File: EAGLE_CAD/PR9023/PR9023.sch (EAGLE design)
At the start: 74 parts, among them SW1 ESWT_TL3315, U1 SI4702-C19-GMR, X1 ABS25XTAL

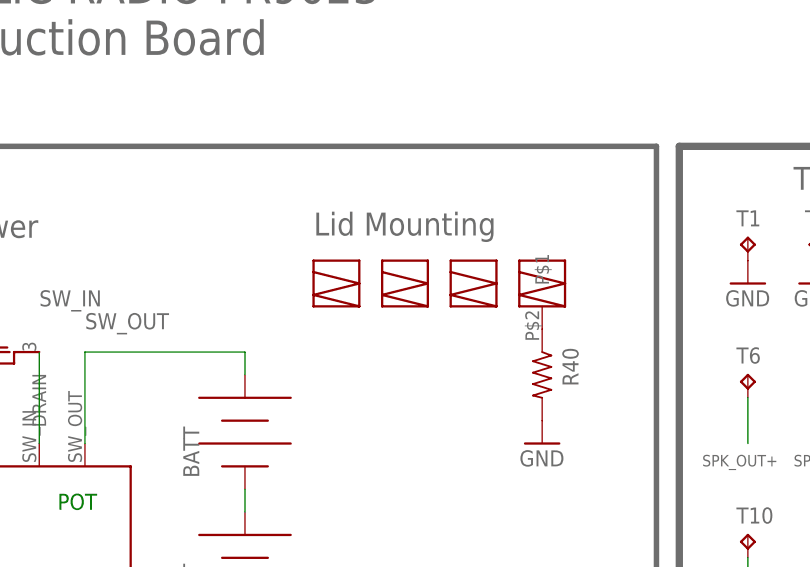
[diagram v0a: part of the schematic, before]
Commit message: first update in a while from my end
the big change here is the speaker footprint itself. i updated that to
fit Fun’s redesign. i also made some smallish changes to the board
perimeter and a few of the things inside it - mostly very small changes.
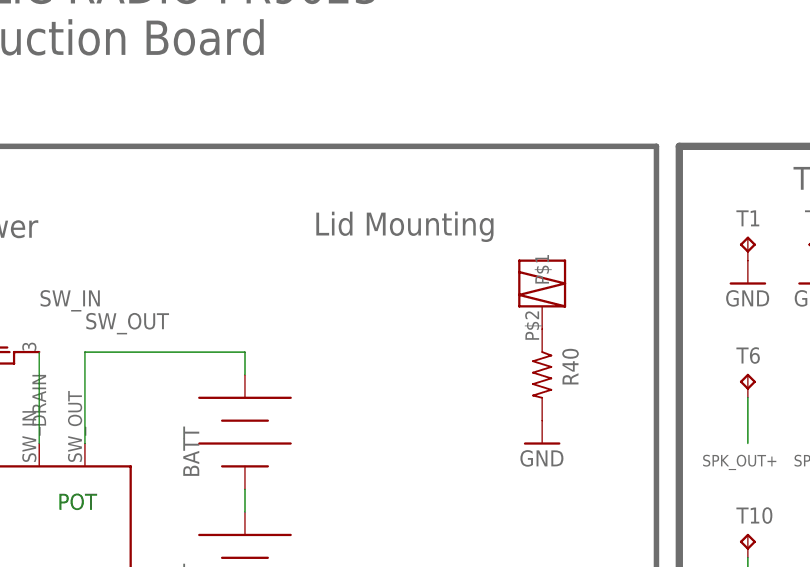
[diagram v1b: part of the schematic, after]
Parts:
- removed U$2, U$3, U$4: PEM_M3_NOPIN, PR_Parts_Library:PEM_M3_NOPIN
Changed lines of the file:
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@@
 <?xml version="1.0" encoding="utf-8"?>
 <!DOCTYPE eagle SYSTEM "eagle.dtd">
-<eagle version="6.6.0">
+<eagle version="7.5.0">
 <drawing>
 <settings>
@@
 <attribute name="MFG_PN" value="ERJ-6GEY0R00V "/>
 </part>
-<part name="U$2" library="PR_Parts_Library" deviceset="PEM_M3_NOPIN" device=""/>
-<part name="U$3" library="PR_Parts_Library" deviceset="PEM_M3_NOPIN" device=""/>
-<part name="U$4" library="PR_Parts_Library" deviceset="PEM_M3_NOPIN" device=""/>
 <part name="U$5" library="PR_Parts_Library" deviceset="PEM_M3_W/PIN" device=""/>
 </parts>
@@
 <attribute name="VALUE" x="237.49" y="24.638" size="1.778" layer="96"/>
 </instance>
-<instance part="U$2" gate="G$1" x="20.32" y="137.16"/>
-<instance part="U$3" gate="G$1" x="27.94" y="137.16"/>
-<instance part="U$4" gate="G$1" x="35.56" y="137.16"/>
 <instance part="U$5" gate="G$1" x="43.18" y="137.16"/>
 </instances>

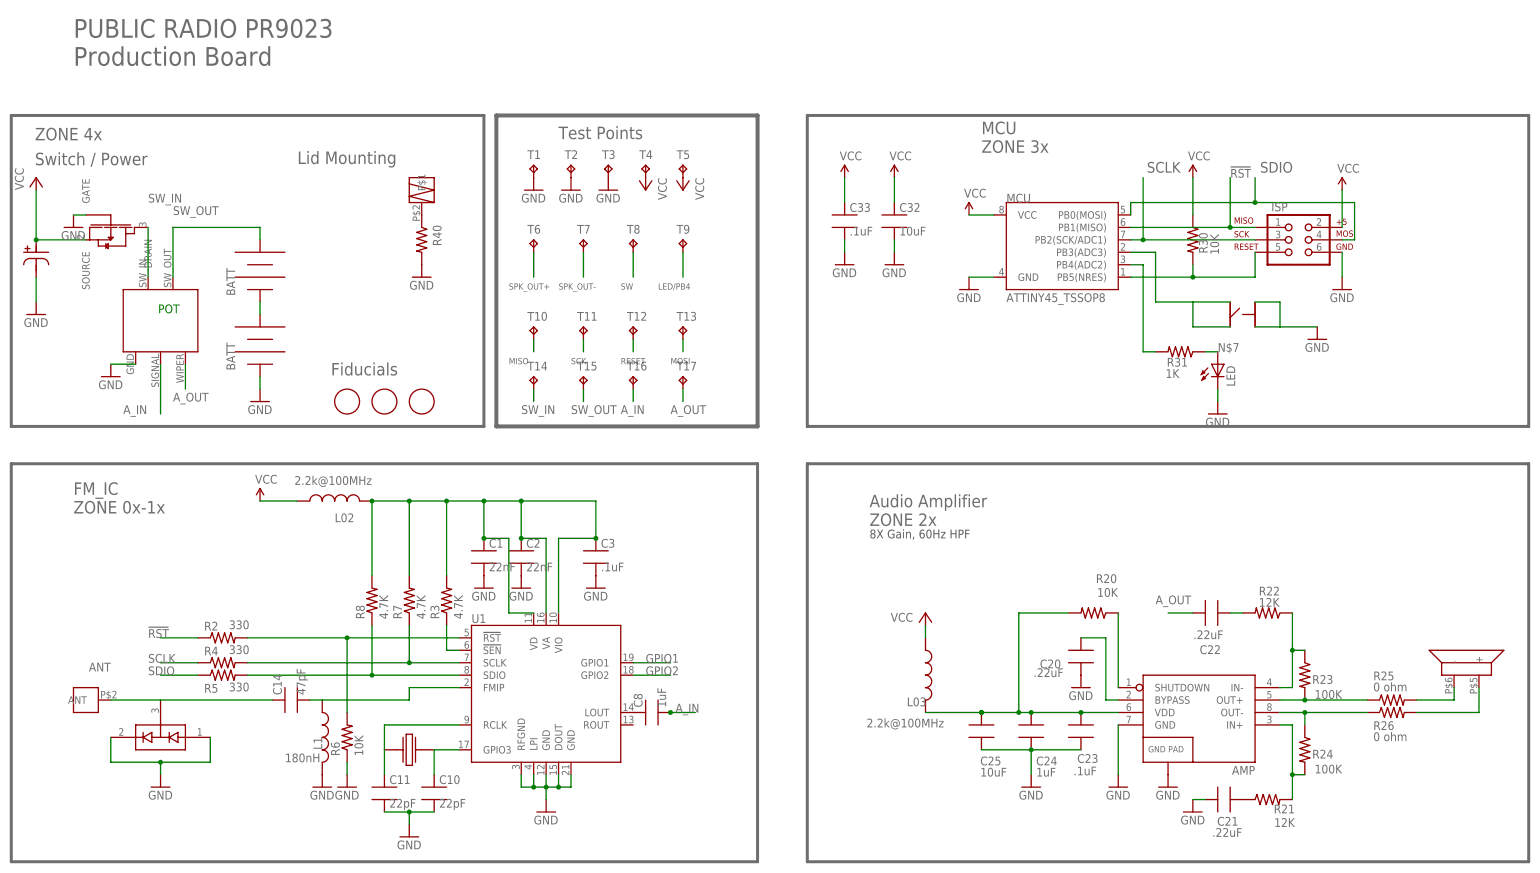
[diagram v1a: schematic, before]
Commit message: Small changes
Added ground to the speaker/lid connection
Modified board outline
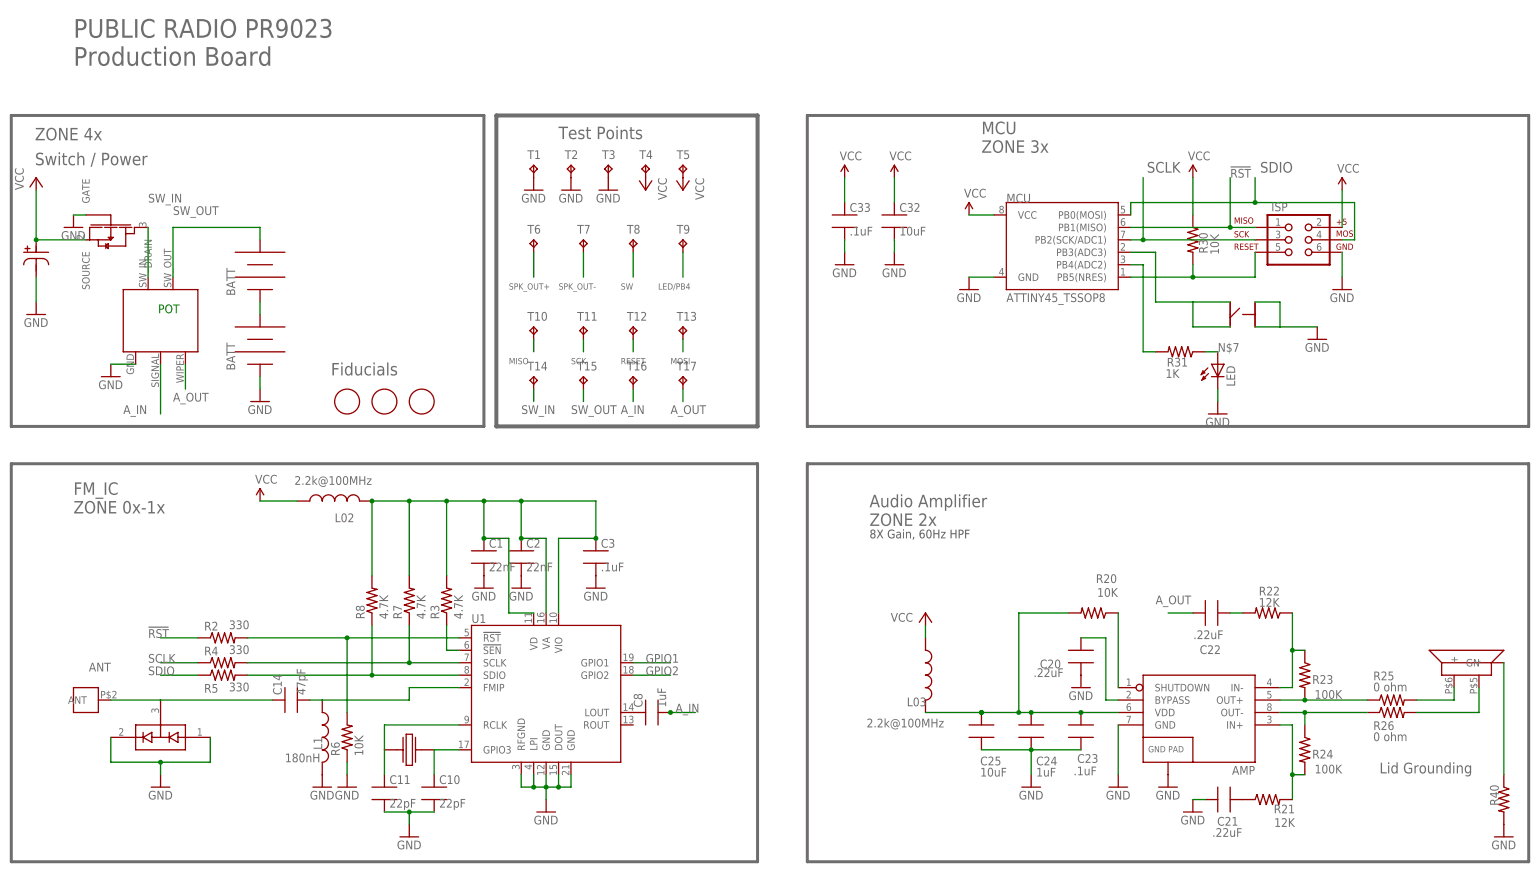
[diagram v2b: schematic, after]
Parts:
- removed U$5: PEM_M3_W/PIN, PR_Parts_Library:PEM_M3_W/PIN
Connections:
- net N$6: now also SPKR_PLACE.GN; no longer U$5.P$1
- net SPK_OUT+: now also SPKR_PLACE.+; no longer SPKR_PLACE.-
- net SPK_OUT-: now also SPKR_PLACE.-; no longer SPKR_PLACE.+
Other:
- note added: "Lid Grounding"
- note removed: "Lid Mounting"
- moved on the sheet: R40
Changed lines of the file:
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@@
 <?xml version="1.0" encoding="utf-8"?>
 <!DOCTYPE eagle SYSTEM "eagle.dtd">
-<eagle version="7.5.0">
+<eagle version="6.6.0">
 <drawing>
 <settings>
@@
 <attribute name="MFG_PN" value="ERJ-6GEY0R00V "/>
 </part>
-<part name="U$5" library="PR_Parts_Library" deviceset="PEM_M3_W/PIN" device=""/>
 </parts>
 <sheets>
@@
 ZONE 0x-1x</text>
 <text x="-35.814" y="142.24" size="2.54" layer="96">Switch / Power  </text>
-<text x="17.78" y="142.494" size="2.54" layer="96">Lid Mounting</text>
+<text x="238.76" y="18.034" size="2.1844" layer="96">Lid Grounding</text>
 <text x="134.62" y="68.58" size="2.54" layer="96">Audio Amplifier
 ZONE 2x</text>
@@
 <instance part="GND5" gate="1" x="-20.32" y="99.06"/>
 <instance part="GND2" gate="1" x="-35.56" y="111.76"/>
-<instance part="GND12" gate="1" x="43.18" y="119.38"/>
+<instance part="GND12" gate="1" x="264.16" y="5.08"/>
 <instance part="GND3" gate="1" x="-27.94" y="129.54"/>
 <instance part="MCU" gate="G$1" x="175.26" y="124.46"/>
@@
 <attribute name="VALUE" x="176.276" y="17.653" size="1.778" layer="96"/>
 </instance>
-<instance part="R40" gate="G$1" x="43.18" y="127" smashed="yes" rot="R270">
-<attribute name="NAME" x="47.2186" y="125.73" size="1.778" layer="95" rot="R90"/>
+<instance part="R40" gate="G$1" x="264.16" y="12.7" smashed="yes" rot="R270">
+<attribute name="NAME" x="263.1186" y="11.43" size="1.778" layer="95" rot="R90"/>
 </instance>
 <instance part="D1" gate="G$1" x="-10.16" y="25.4" rot="R180"/>
@@
 <attribute name="VALUE" x="237.49" y="24.638" size="1.778" layer="96"/>
 </instance>
-<instance part="U$5" gate="G$1" x="43.18" y="137.16"/>
 </instances>
 <busses>
@@
 <wire x1="246.38" y1="33.02" x2="254" y2="33.02" width="0.1524" layer="91"/>
 <pinref part="R25" gate="G$1" pin="2"/>
-<pinref part="SPKR_PLACE" gate="G$1" pin="-"/>
+<pinref part="SPKR_PLACE" gate="G$1" pin="+"/>
 <wire x1="254" y1="33.02" x2="254" y2="35.56" width="0.1524" layer="91"/>
 </segment>
@@
 <segment>
 <pinref part="R26" gate="G$1" pin="2"/>
-<pinref part="SPKR_PLACE" gate="G$1" pin="+"/>
 <wire x1="246.38" y1="30.48" x2="259.08" y2="30.48" width="0.1524" layer="91"/>
+<pinref part="SPKR_PLACE" gate="G$1" pin="-"/>
 <wire x1="259.08" y1="30.48" x2="259.08" y2="35.56" width="0.1524" layer="91"/>
 </segment>
@@
 <net name="N$6" class="0">
 <segment>
+<pinref part="SPKR_PLACE" gate="G$1" pin="GN"/>
 <pinref part="R40" gate="G$1" pin="1"/>
-<pinref part="U$5" gate="G$1" pin="P$1"/>
-</segment>
-</net>
+<wire x1="264.16" y1="40.64" x2="264.16" y2="17.78" width="0.1524" layer="91"/>
+</segment>
+</net>
